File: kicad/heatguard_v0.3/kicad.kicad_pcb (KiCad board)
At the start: 2 copper layers, 100 x 82 mm, 31 parts, among them J1 Conn_02x02_Odd_Even, J20 Conn_01x01, J7 Conn_01x12, J8 Conn_02x04_Odd_Even, J9 Conn_02x04_Odd_Even, U1 LM75B, U2 LM75B, U3 M24C02-FMN, U4 XIAO-RP2040-DIP

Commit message: Changes v0.2 -> v0.3 A
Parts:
- added Logo_open_hardware101: Logo_Open_Hardware_Small, Symbol:OSHW-Logo2_9.8x8mm_SilkScreen, F.Cu at (54.5, 124.2)
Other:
- board text added: "Controller"
- board text added: "DIAG_RX - GPIO_PROBE_4 DIAG_TX - GPIO_PROBE_5"
- board text added: "Small font: Testinterface. Inject (stimuli) or Probe"
- board text added: "testing NOT required"
- board text removed: "DIAG_RX - GPIO_PROBE_5 DIAG_TX - GPIO_PROBE_4"
- board text removed: "Small font: Testinterface. Inject (stimuly) or Probe"

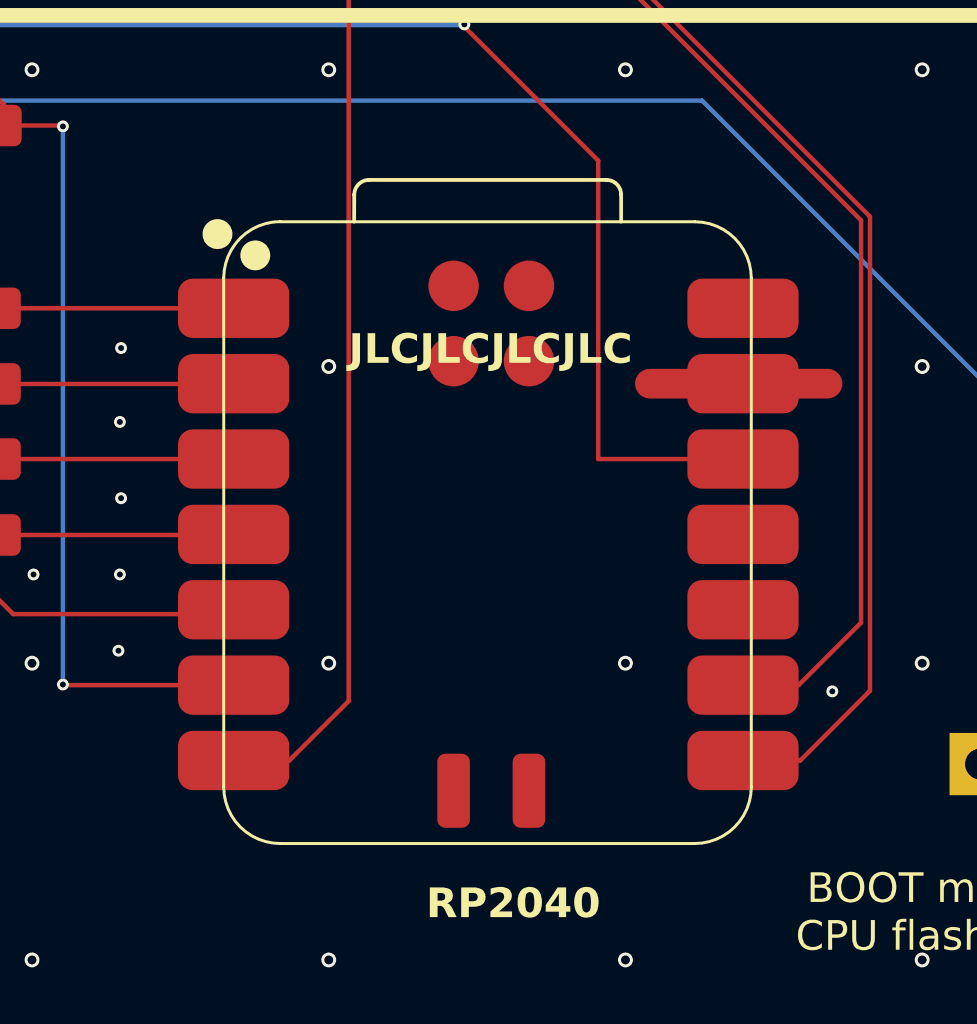
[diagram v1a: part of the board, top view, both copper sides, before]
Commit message: Changes v0.2 -> v0.3 B: PCB: XIAO rp2040: Replace SMD with THT
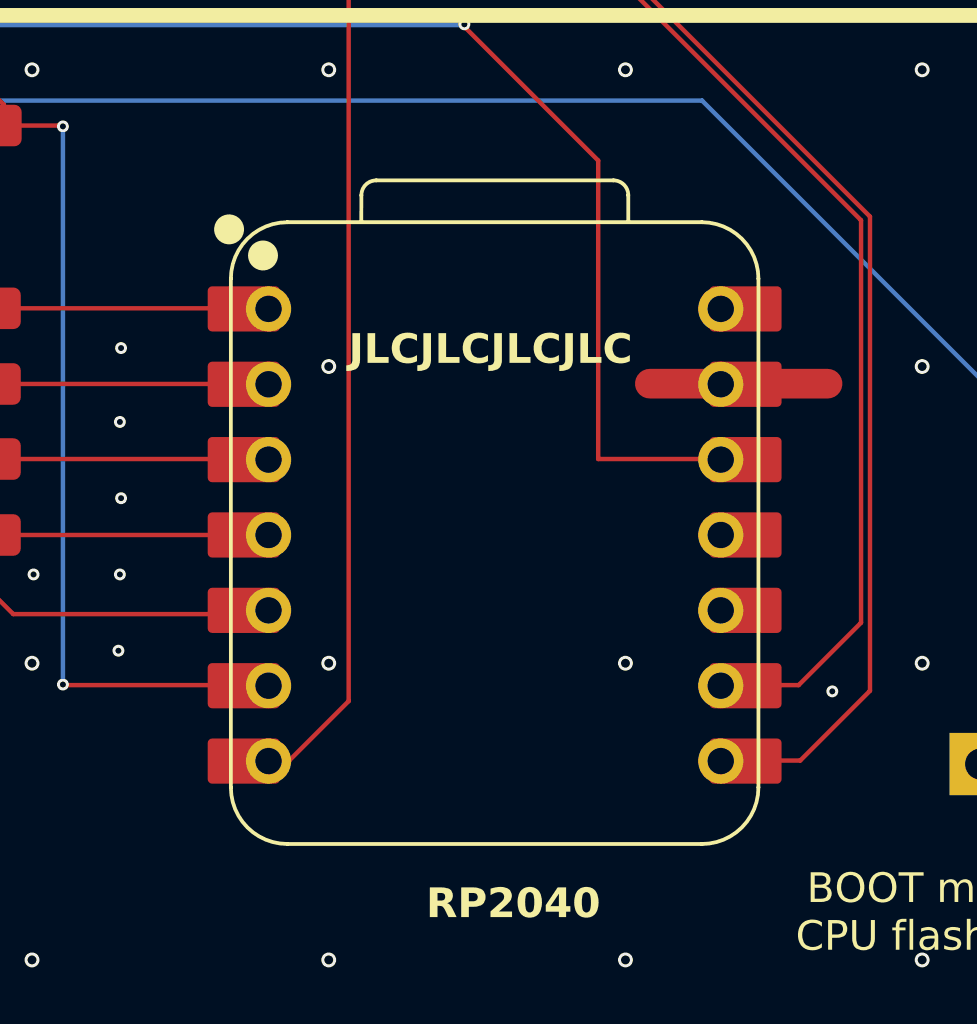
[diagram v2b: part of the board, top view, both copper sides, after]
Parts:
- U4: footprint 00_project_library:XIAO-RP2040-SMD -> 00_project_library:XIAO-RP2040-DIP
- moved U4 13.9 mm to (127.4, 87.7), turned to 90 degrees

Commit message: Changes v0.2 -> v0.3 C: Use relays in favor of GPIO
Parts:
- removed J1: Conn_02x02_Odd_Even, 00_project_library:PinHeader_2x02_P2.54mm_Vertical_back
- added J2: Conn_02x12_Odd_Even, 00_project_library:PinHeader_2x12_P2.54mm_Vertical_back, F.Cu at (50.5, 55.7)
- moved Logo_open_hardware101 104.4 mm to (141.2, 66.0)
- moved R9 12.4 mm to (77.5, 71.8), turned to 180 degrees
- moved R7 12.3 mm to (66.9, 71.8), turned to 180 degrees
- moved R8 12.2 mm to (72.2, 71.8)
- moved R10 9.79 mm to (82.8, 71.8), turned to 0 degrees
- moved J7 3.19 mm to (118.2, 66.4)
- moved R6 0.42 mm to (109.9, 74.3)
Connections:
- J8 pad 1: /inject_tguard_disconnect -> unconnected-(J8-Pin_1-Pad1)
- J8 pad 2: /inject_tref_disconnect -> unconnected-(J8-Pin_2-Pad2)
- J8 pad 3: /inject_T_limit -> unconnected-(J8-Pin_3-Pad3)
- J8 pad 4: /inject_eeprom_disconnect -> unconnected-(J8-Pin_4-Pad4)
- J8 pad 5: /DIAG_RX -> unconnected-(J8-Pin_5-Pad5)
- J8 pad 7: /DIAG_TX -> unconnected-(J8-Pin_7-Pad7)
- U4 pad 10: unconnected-(U4-P4_D9_MISO-Pad10) -> /watchdog_disable
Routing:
- net /watchdog_disable: track 0.00 -> 110.3 mm, vias 0 -> 1
- net Net-(J2-Pin_10): track 0.00 -> 49.0 mm
- net /DIAG_RX: track 79.5 -> 48.5 mm, vias 2 -> 0
- net /DIAG_TX: track 63.8 -> 35.2 mm
- net /inject_tref_disconnect: track 68.1 -> 48.5 mm
- net /inject_eeprom_disconnect: track 95.7 -> 89.5 mm, vias 4 -> 3
- net /inject_tguard_disconnect: track 74.9 -> 70.1 mm
- net GND: track 5.99 -> 9.89 mm, vias 81 -> 70
- net /inject_T_limit: track 167.0 -> 169.9 mm
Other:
- outline, holes or cut-outs redrawn
- board text added: "DIAG_RX GPIO_PROBE_4 DIAG_TX GPIO_PROBE_5"
- board text added: "I2C"
- board text added: "bootmode CPU flash"
- board text added: "eeprom"
- board text added: "inject_ T_limit"
- board text added: "inject_XX_disconnect"
- board text added: "tguard"
- board text added: "tref"
- board text added: "watchdog_ disable"
- board text removed: "1b"
- board text removed: "DIAG_RX - GPIO_PROBE_4 DIAG_TX - GPIO_PROBE_5"
- board text removed: "GND"
- board text removed: "inject_xx_disconnect Tref/EEPROM Tguard/T_limit"
- board text removed: "protocols I2C_SDA/I2C_SCL DIAG_RX/DIAG_TX"
